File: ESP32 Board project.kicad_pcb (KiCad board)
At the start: 4 copper layers, 86.5 x 51.5 mm, 89 parts, among them J1 SS-52400-002, J2 B2B-PH-SM4-TB, J3 GSD090012SEU, J4 Conn_01x04_Pin, J6 Conn_01x05_Pin, Q1 TEMT6000X01, Q2 BC817, Q3 BC817, U1 MCP73871-2CAI_ML, U2 BME280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

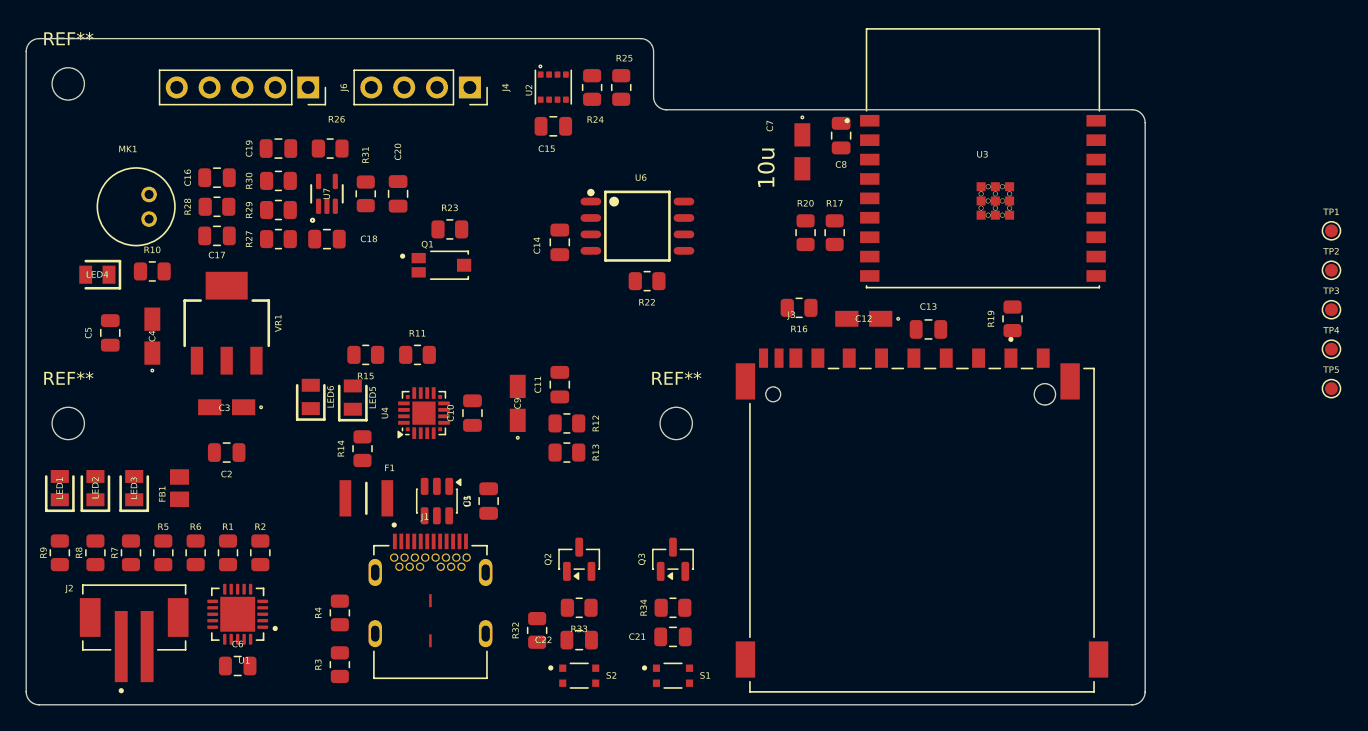
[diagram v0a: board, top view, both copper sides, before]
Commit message: PCB: added copper zones
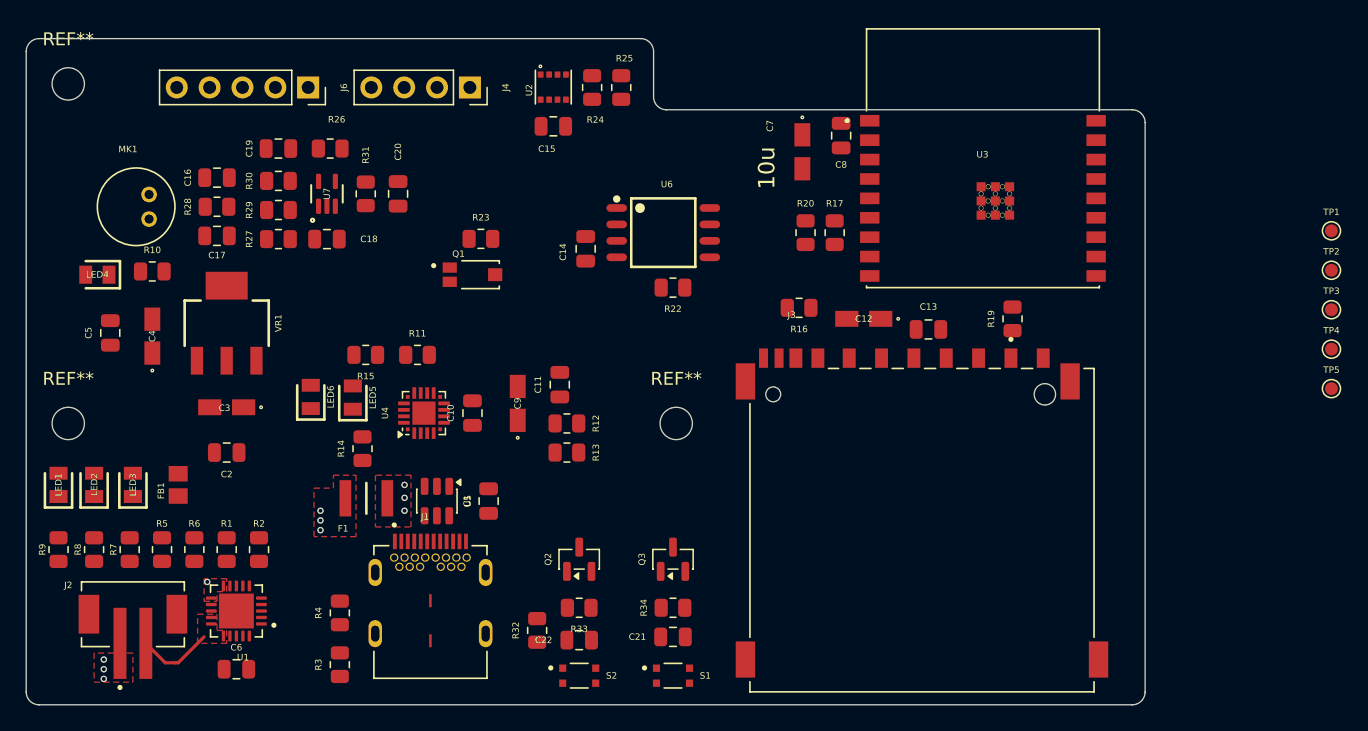
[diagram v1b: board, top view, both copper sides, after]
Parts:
- moved Q1 2.51 mm to (188.2, 77.0)
- moved R23 2.51 mm to (188.9, 74.2)
- moved C14 2.06 mm to (197.0, 75.0)
- moved R22 2.06 mm to (203.8, 78.0)
- moved U6 2.06 mm to (203.0, 73.8)
- moved C6 0.27 mm to (170.0, 107.5)
- moved FB1 0.27 mm to (165.5, 93.2)
- moved J2 0.27 mm to (162.0, 103.2)
- moved LED1 0.27 mm to (156.2, 93.2)
- moved LED2 0.27 mm to (159.0, 93.2)
- moved LED3 0.27 mm to (162.0, 93.2)
- moved R1 0.27 mm to (169.2, 98.2)
- moved R2 0.27 mm to (171.8, 98.2)
- moved R5 0.27 mm to (164.2, 98.2)
- moved R6 0.27 mm to (166.8, 98.2)
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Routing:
- net /VBAT: track 0.00 -> 5.95 mm
- net GND: vias 0 -> 4
- net /VBUS: vias 0 -> 3
- net /+5V_USB: vias 0 -> 3
- added copper zone on F.Cu, net /+5V_USB
- added copper zone on F.Cu, net /VBAT
- added copper zone on F.Cu, net /VBUS
- added copper zone on F.Cu, net GND

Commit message: Updated SPI connection and +5V connection
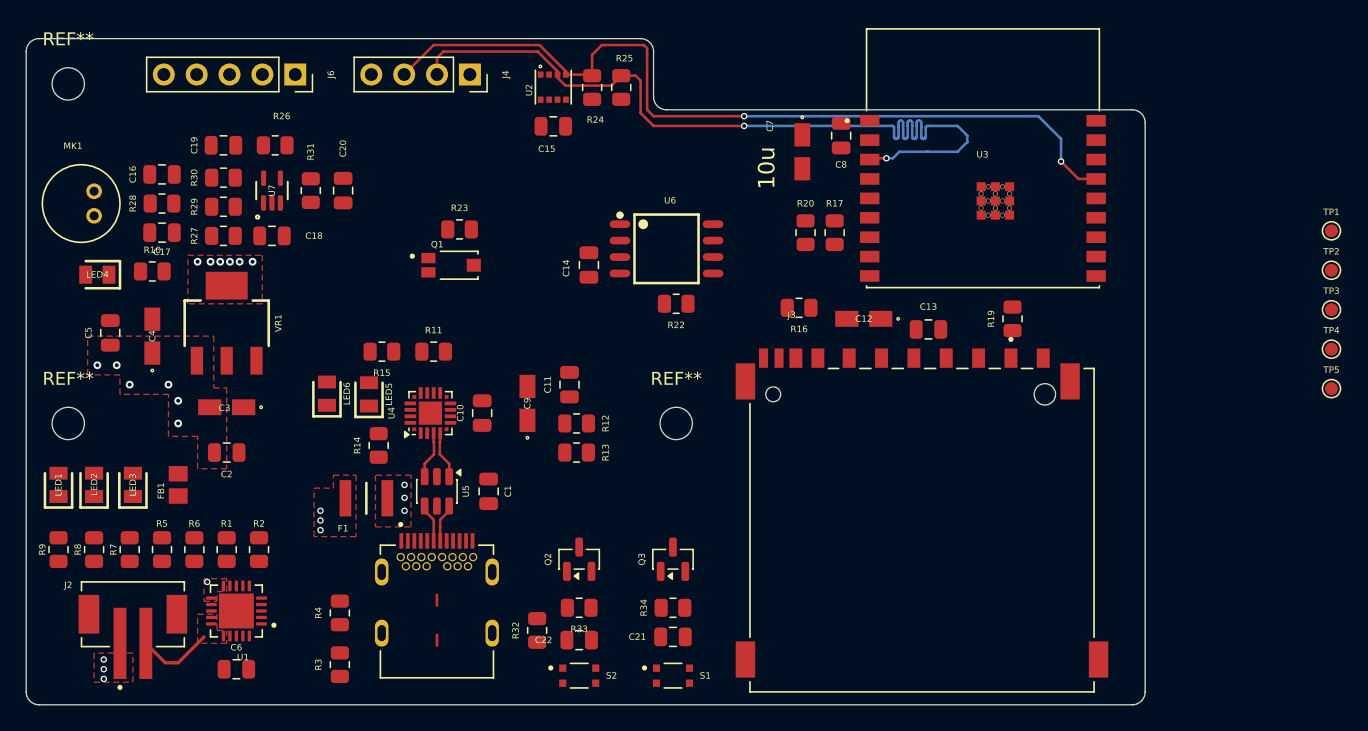
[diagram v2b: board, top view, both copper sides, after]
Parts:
- moved C16 4.26 mm to (164.2, 69.2)
- moved C17 4.26 mm to (164.2, 73.8)
- moved C18 4.26 mm to (172.8, 74.0)
- moved C19 4.26 mm to (169.0, 67.0)
- moved C20 4.26 mm to (178.2, 70.5)
- moved MK1 4.26 mm to (158.0, 71.5)
- moved R26 4.26 mm to (173.0, 67.0)
- moved R27 4.26 mm to (169.0, 74.0)
- moved R28 4.26 mm to (164.2, 71.5)
- moved R29 4.26 mm to (169.0, 71.8)
- moved R30 4.26 mm to (169.0, 69.5)
- moved R31 4.26 mm to (175.8, 70.5)
- moved U7 4.26 mm to (172.8, 70.5)
- moved Q1 1.81 mm to (186.6, 76.3)
- moved R23 1.81 mm to (187.2, 73.5)
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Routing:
- net /ESP32-C3-02/SCL: track 0.00 -> 65.6 mm, vias 0 -> 2
- net /ESP32-C3-02/SDA: track 0.00 -> 65.5 mm, vias 0 -> 2
- net /ESP32-C3-02/USB_D-: track 0.00 -> 4.09 mm
- net /ESP32-C3-02/USB_D+: track 0.00 -> 3.67 mm
- net /USB_DP: track 0.00 -> 3.15 mm
- net /USB_DN: track 0.00 -> 2.99 mm
- net GND: track 0.00 -> 0.07 mm, vias 4 -> 10
- net +3.3V: vias 0 -> 6
- added copper zone on F.Cu, net (none)
